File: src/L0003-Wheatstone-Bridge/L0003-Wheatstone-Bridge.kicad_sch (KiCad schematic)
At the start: 18 parts, among them P1 12V, P2 2043-1X04G00DAU, U1 MCP1703T-4002E_DB

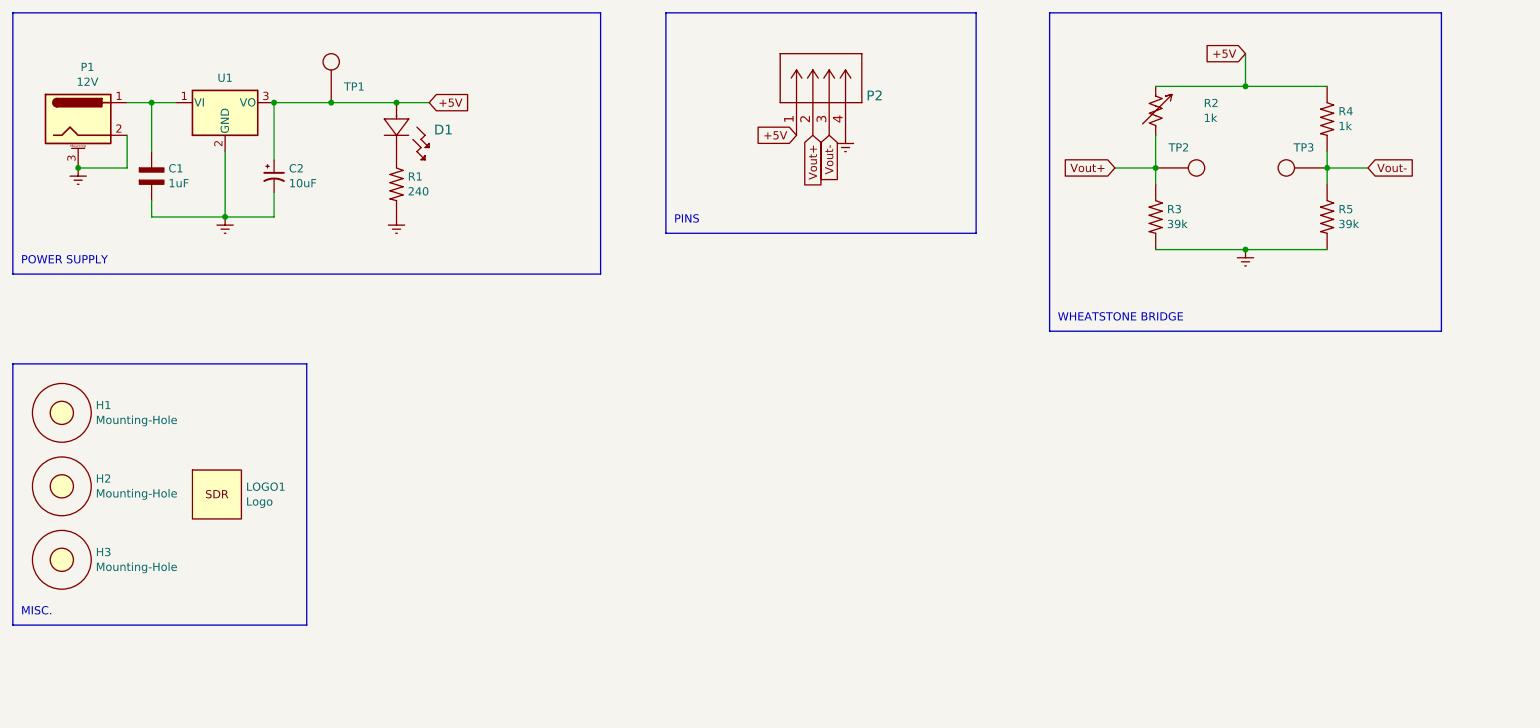
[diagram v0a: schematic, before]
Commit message: added PT connectors for engine controller compatibility
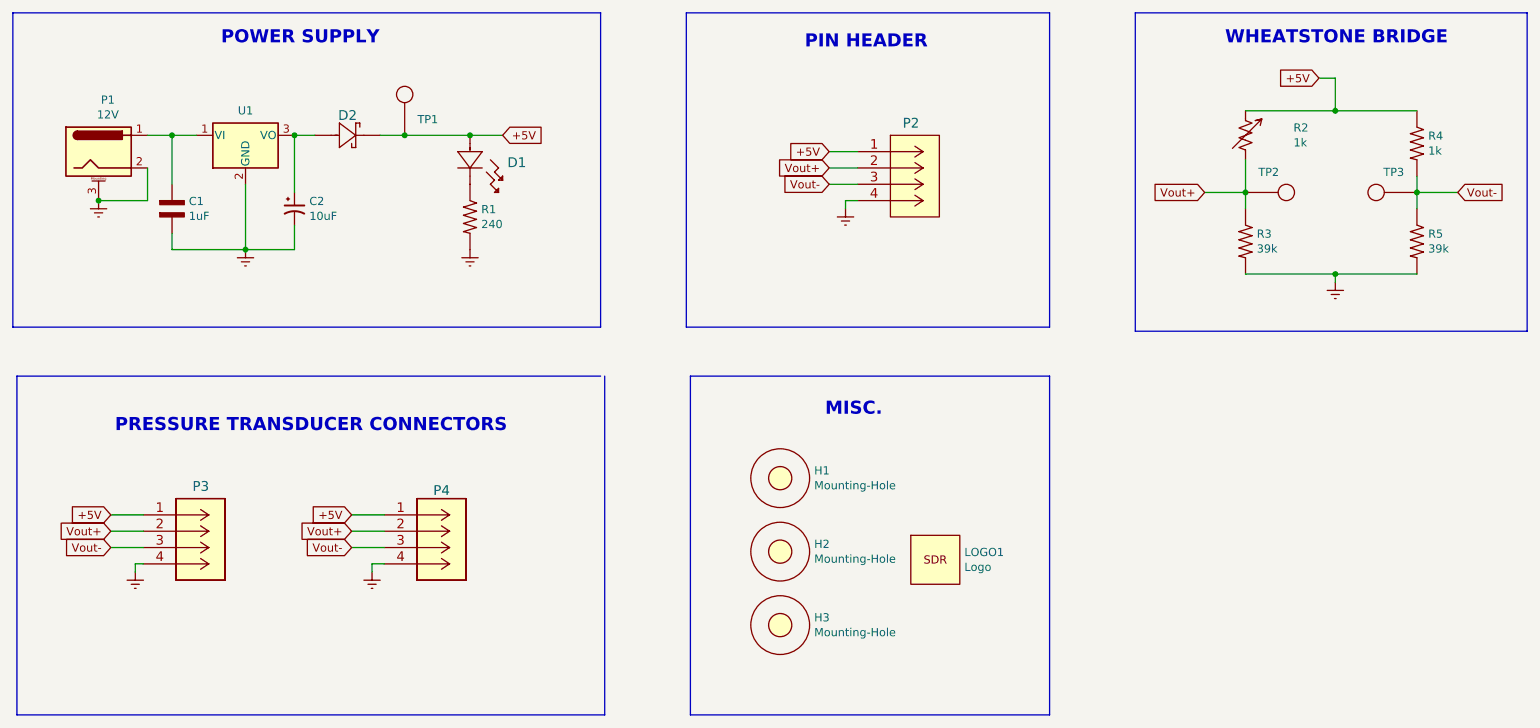
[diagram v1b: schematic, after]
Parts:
- removed P2: 2043-1X04G00DAU, L0003-Wheatstone-Bridge:SULLINS_PPTC041LFBN-RC, symbol L0003-Wheatstone-Bridge:2043-1X04G00DAU
- added D2: SM5819PL-TP, L0003-Wheatstone-Bridge:SM5819PL-TP, symbol L0003-Wheatstone-Bridge:SM5819PL-TP
- added P2: PPTC041LFBN-RC, L0003-Wheatstone-Bridge:PPTC041LFBN-RC, symbol L0003-Wheatstone-Bridge:PPTC041LFBN-RC
- added P3, P4: 39299043, L0003-Wheatstone-Bridge:39299043, symbol L0003-Wheatstone-Bridge:39299043
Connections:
- net +5V: now also D2.1, P2.1, P3.1 (+12V), P4.1 (+12V); no longer C2.1, U1.3 (VO)
- net Earth: now also P2.4, P3.4, P4.4
- net Vout+: now also P2.2, P3.2 (GND), P4.2 (GND)
- net Vout-: now also P2.3, P3.3, P4.3
- new net: C2.1, D2.2, U1.3 (VO)
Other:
- note added: "PIN HEADER"
- note added: "PRESSURE TRANSDUCER CONNECTORS"
- note removed: "PINS"
- moved on the sheet: C1, C2, D1, H1, H2, H3, LOGO1, P1, R1, R2, R3, R4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

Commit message: updated schematic with new resistor values
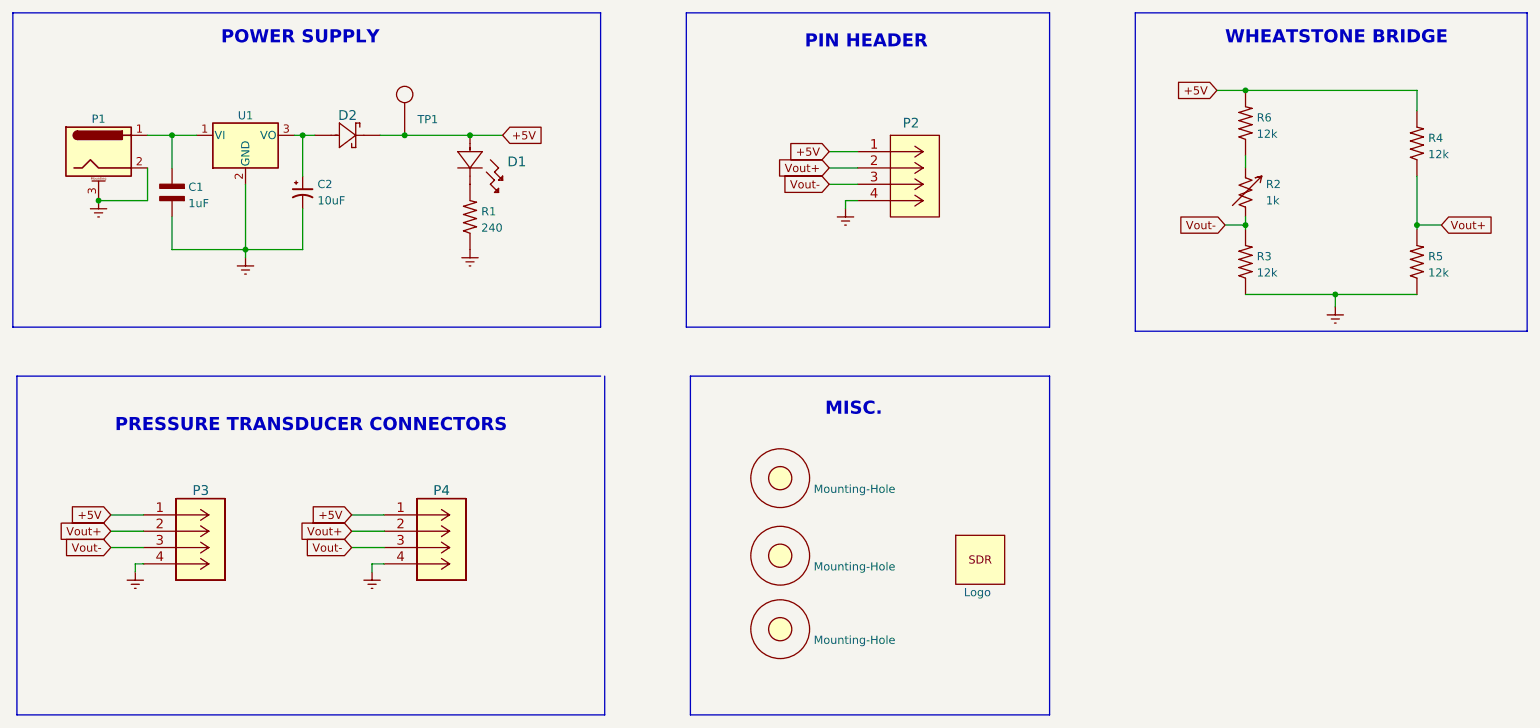
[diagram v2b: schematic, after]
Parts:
- removed TP2: TP2, L0003-Wheatstone-Bridge:TP, symbol L0003-Wheatstone-Bridge:TP
- removed TP3: TP3, L0003-Wheatstone-Bridge:TP, symbol L0003-Wheatstone-Bridge:TP
- added R6: 12k, symbol L0003-Wheatstone-Bridge:RES_0603
- C1: footprint L0003-Wheatstone-Bridge:CAP_0603 -> (none)
- C2: footprint L0003-Wheatstone-Bridge:T491A106K010AT -> (none)
- D1: footprint L0003-Wheatstone-Bridge:SML-LX1206GC-TR -> (none)
- H1, H2, H3: footprint L0003-Wheatstone-Bridge:MountingHole_2.1mm -> (none)
- LOGO1: footprint L0003-Wheatstone-Bridge:logo2 -> (none)
- P1: value 12V -> EJ508A; footprint L0003-Wheatstone-Bridge:12V_power_jack -> (none)
- P3, P4: footprint L0003-Wheatstone-Bridge:39299043 -> CONN_4840.2201_SCH
- R1: footprint L0003-Wheatstone-Bridge:RES_0603 -> (none)
- R2: footprint L0003-Wheatstone-Bridge:TRIM_3310Y-001-102L -> (none)
- R3, R5: value 39k -> 12k; footprint L0003-Wheatstone-Bridge:RES_0603 -> (none)
- R4: value 1k -> 12k; footprint L0003-Wheatstone-Bridge:RES_0603 -> (none)
- U1: footprint L0003-Wheatstone-Bridge:MCP1703T-4002E&slash_DB -> Package_TO_SOT_SMD:SOT-223-3_TabPin2
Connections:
- net +5V: now also R4.2, R6.2; no longer R2.1, R4.1
- net Earth: now also C1.2, R1.1, R3.1, R5.1; no longer C1.1, R1.2, R3.2, R5.2
- net Vout+: now also R4.1, R5.2; no longer R2.2, R3.1
- net Vout-: now also R2.2, R3.2; no longer R4.2, R5.1
- net at P1.1, U1.1 (VI): now also C1.1; no longer C1.2
- net at D1.1: now also R1.2; no longer R1.1
- new net: R2.1, R6.1
